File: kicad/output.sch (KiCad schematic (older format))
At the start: 6 parts, among them J4 OUT, Q6 2N3904

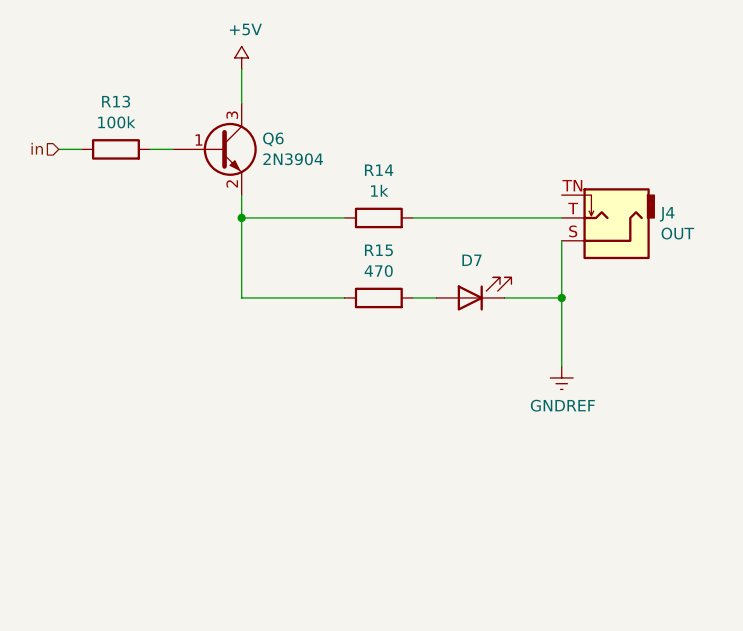
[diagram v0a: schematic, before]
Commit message: Use 6V. Add output diodes + output pin headers
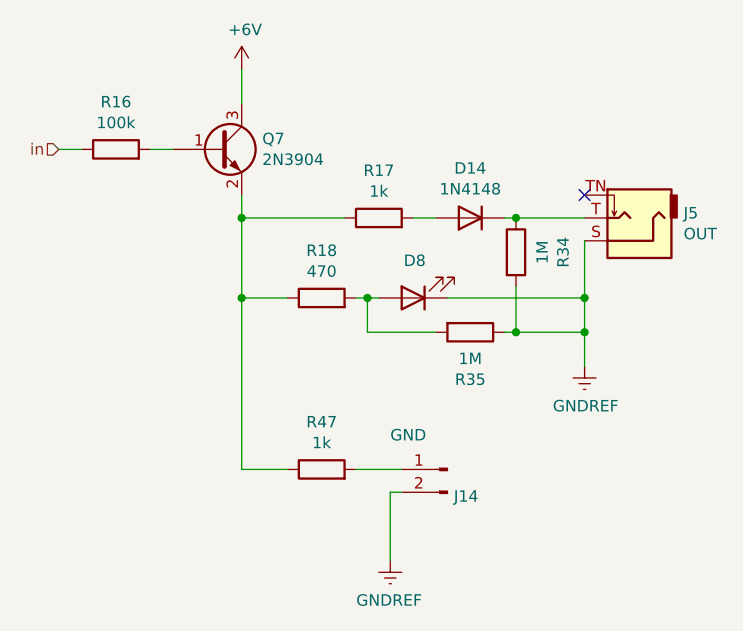
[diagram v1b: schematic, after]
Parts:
- added D14: 1N4148, Diode_SMD:D_SOD-123, symbol Device:D
- added J17: GND, Connector_PinHeader_2.54mm:PinHeader_1x02_P2.54mm_Vertical, symbol Connector:Conn_01x02_Male
- added R32, R33: 1M, Resistor_SMD:R_0402_1005Metric, symbol Device:R
- added R46: 1k, Resistor_SMD:R_0402_1005Metric, symbol Device:R
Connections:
- net GNDREF: now also J17.2 (Pin_2), R32.2, R33.1
- net at Q6.2 (E), R14.1, R15.1: now also R46.1
- net at R14.2: now also D14.2 (A); no longer J4.T
- net at D7.2 (A), R15.2: now also R33.2
- net +5V renamed +6V
- new net: D14.1 (K), J4.T, R32.1
- new net: J17.1 (Pin_1), R46.2
- no-connect marks 0 -> 1
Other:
- moved on the sheet: D8, J5, R18
